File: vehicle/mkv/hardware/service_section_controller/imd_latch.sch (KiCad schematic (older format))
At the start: 36 parts, among them J301 UF_5_VT, K301 G5Q-1A4-DC12, Q301 SSM3K333R, Q302 SSM3K333R, U301 TLV3701QDBVRG4Q1, U302 TLV3701QDBVRG4Q1, U303 CD4044BDR

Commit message: incorporated feedback from dr
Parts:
- renumbered R313 to R312, R314 to R313, R315 to R314, R312 to R315, U303 to U?
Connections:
- net labels added: +12V_IMD, +12V_SHUTDOWN
- net labels removed: 12V_IMD, 12V_SHUTDOWN
- wire segments 107 -> 106
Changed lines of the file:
@@
 Wire Wire Line
 	9800 3850 9800 3750
-Wire Wire Line
-	9500 3000 9500 3150
 Text Notes 8900 2800 0    98   ~ 0
 IMD Shutdown Relay
@@
 $EndComp
 Wire Wire Line
-	9500 4900 9500 5000
+	9500 4950 9500 5000
 $Comp
 L power:GND #PWR?
@@
 I _lim: 20mA\n
 $Comp
-L formula:R_1K R312
+L formula:R_1K R315
 U 1 1 610EBBF8
 P 9500 5150
-F 0 "R312" H 9570 5196 50  0000 L CNN
+F 0 "R315" H 9570 5196 50  0000 L CNN
 F 1 "R_1K" H 9570 5105 50  0000 L CNN
 F 2 "footprints:R_0805_OEM" H 9430 5150 50  0001 C CNN
@@
 Wire Wire Line
 	10300 3850 9800 3850
-Text GLabel 9500 4900 2    50   Input ~ 0
-12V_IMD
-Text GLabel 9500 3000 0    50   Input ~ 0
-12V_SHUTDOWN
 Text Label 8100 5000 2    50   ~ 0
 LATCH_OUTPUT
@@
 	8250 5350 8250 5400
 NoConn ~ 5650 2000
-Text Notes 5100 3100 0    50   ~ 0
+Text Notes 5050 3350 0    50   ~ 0
 Latch outputs 12V when the IMD Output is “Healthy”
 Text Notes 5900 1600 0    50   ~ 0
@@
 Wire Wire Line
 	6750 1500 6750 1400
-Wire Wire Line
-	6750 1900 6900 1900
 Connection ~ 6750 1900
 Wire Wire Line
@@
 	1    0    0    -1
 $EndComp
-Text GLabel 6900 1900 2    50   Input ~ 0
-12V_IMD
 Wire Wire Line
 	7650 2000 7650 2150
@@
 NoConn ~ 6600 2500
 $Comp
-L formula:CD4044BDR U303
+L formula:CD4044BDR U?
 U 1 1 60D455EC
 P 6350 2600
-F 0 "U303" H 6125 3525 50  0000 C CNN
+F 0 "U?" H 6125 3525 50  0000 C CNN
 F 1 "CD4044BDR" H 6125 3434 50  0000 C CNN
 F 2 "footprints:SOIC127P600X175-16N" H 5850 1850 50  0001 L BNN
@@
 NoConn ~ 5650 1900
 Wire Wire Line
-	5650 2300 4950 2300
-Text GLabel 4950 2900 2    50   Input ~ 0
-12V_IMD
+	5650 2300 5350 2300
 Wire Wire Line
 	5650 2600 5550 2600
@@
 Wire Wire Line
 	1750 3700 2350 3700
-Wire Wire Line
-	1750 3700 1475 3700
 Wire Wire Line
 	2950 3900 3275 3900
@@
 	2950 4700 2650 4700
 Wire Wire Line
-	1900 4700 2000 4700
-Wire Wire Line
 	2300 4700 2350 4700
 $Comp
@@
 	0    1    1    0
 $EndComp
-Text GLabel 1900 4700 0    50   Input ~ 0
-12V_IMD
 Wire Wire Line
 	3475 3450 3550 3450
@@
 Wire Wire Line
 	3450 3450 3475 3450
-Wire Wire Line
-	3450 3200 3450 3450
 $Comp
 L formula:C_0.1uF C303
@@
 	0    1    1    0
 $EndComp
-Text GLabel 3450 3200 0    50   Input ~ 0
-12V_IMD
-Wire Wire Line
-	1475 3900 1700 3900
-Text GLabel 1700 3900 2    50   Input ~ 0
-12V_IMD
-Wire Wire Line
-	1475 4000 2000 4000
-Wire Wire Line
-	2000 4150 2000 4000
-$Comp
-L formula:UF_5_VT J301
-U 1 1 610EBAFC
-P 1125 3900
-F 0 "J301" H 1233 4337 60  0000 C CNN
-F 1 "UF_5_VT" H 1233 4231 60  0000 C CNN
-F 2 "footprints:Ultrafit_5" H 1025 4150 60  0001 C CNN
-F 3 "http://www.literature.molex.com/SQLImages/kelmscott/Molex/PDF_Images/987651-1008.pdf" H 1125 4250 60  0001 C CNN
-F 4 "DK" H 1125 3900 60  0001 C CNN "MFN"
-F 5 "WM11667-ND" H 1125 3900 60  0001 C CNN "MPN"
-F 6 "https://www.digikey.com/product-detail/en/molex-llc/1722861105/WM11667-ND/5360132" H 1625 4750 60  0001 C CNN "PurchasingLink"
-	1    1125 3900
-	1    0    0    -1
-$EndComp
 Text Notes 1350 4100 1    50   ~ 0
 This is IMD\n\n
@@
 	2350 3850 2350 3700
 Wire Wire Line
-	1825 4150 1825 4100
-$Comp
-L power:GND #PWR?
-U 1 1 610EBB0C
-P 2000 4150
-F 0 "#PWR?" H 2000 3900 50  0001 C CNN
-F 1 "GND" H 2005 3977 50  0000 C CNN
-F 2 "" H 2000 4150 50  0001 C CNN
-F 3 "" H 2000 4150 50  0001 C CNN
-	1    2000 4150
-	1    0    0    -1
-$EndComp
-$Comp
-L power:GND #PWR?
-U 1 1 610EBB06
-P 1825 4150
-F 0 "#PWR?" H 1825 3900 50  0001 C CNN
-F 1 "GND" H 1830 3977 50  0000 C CNN
-F 2 "" H 1825 4150 50  0001 C CNN
-F 3 "" H 1825 4150 50  0001 C CNN
-	1    1825 4150
-	1    0    0    -1
-$EndComp
-Wire Wire Line
 	2175 3800 2175 4150
-Wire Wire Line
-	1475 4100 1825 4100
-Wire Wire Line
-	1475 3800 2175 3800
 $Comp
 L power:GND #PWR?
@@
 	2100 1150 2150 1150
 Wire Wire Line
-	3400 1450 3400 1750
-Text GLabel 3400 1450 0    50   Input ~ 0
-12V_IMD
-Wire Wire Line
-	1400 2050 1525 2050
-Wire Wire Line
-	1500 1150 1400 1150
-Text GLabel 1400 1150 0    50   Input ~ 0
-12V_IMD
-Text GLabel 1400 2050 0    50   Input ~ 0
-12V_IMD
+	1250 2050 1525 2050
+Wire Wire Line
+	1500 1150 1250 1150
 Wire Wire Line
 	2125 2050 2250 2050
@@
 	9050 3850 9050 3650
 $Comp
-L formula:R_1.13K R315
+L formula:R_1.13K R314
 U 1 1 60D069DE
 P 8750 6050
-F 0 "R315" H 8820 6096 50  0000 L CNN
+F 0 "R314" H 8820 6096 50  0000 L CNN
 F 1 "R_1.13K" H 8820 6005 50  0000 L CNN
 F 2 "footprints:R_0805_OEM" H 8680 6050 50  0001 C CNN
@@
 	8250 5000 8750 5000
 $Comp
-L formula:R_2.2K R313
+L formula:R_2.2K R312
 U 1 1 60D03BAD
 P 8750 5200
-F 0 "R313" H 8820 5246 50  0000 L CNN
+F 0 "R312" H 8820 5246 50  0000 L CNN
 F 1 "R_2.2K" H 8820 5155 50  0000 L CNN
 F 2 "footprints:R_0805_OEM" H 8680 5200 50  0001 C CNN
@@
 $EndComp
 $Comp
-L formula:R_1K R314
+L formula:R_1K R313
 U 1 1 60DAD819
 P 8750 5550
-F 0 "R314" H 8820 5596 50  0000 L CNN
+F 0 "R313" H 8820 5596 50  0000 L CNN
 F 1 "R_1K" H 8820 5505 50  0000 L CNN
 F 2 "footprints:R_0805_OEM" H 8680 5550 50  0001 C CNN
@@
 Wire Wire Line
 	4750 2200 5650 2200
-Wire Wire Line
-	4950 2300 4950 2900
 Wire Wire Line
 	4750 2200 4750 3800
@@
 U 1 1 6147DE08
 P 2650 2000
-F 0 "TP302" V 2650 2250 50  0000 C CNN
+F 0 "TP302" V 2650 2300 50  0000 C CNN
 F 1 "Test_Point_SMD" V 2550 2050 50  0000 C CNN
 F 2 "TestPoint:TestPoint_Pad_D1.0mm" H 2650 1850 50  0001 C CNN
@@
 Wire Wire Line
 	9800 2950 9800 3150
+Wire Wire Line
+	1475 3800 2175 3800
+Wire Wire Line
+	1750 3700 1475 3700
+$Comp
+L formula:UF_5_VT J301
+U 1 1 610EBAFC
+P 1125 3900
+F 0 "J301" H 1233 4337 60  0000 C CNN
+F 1 "UF_5_VT" H 1233 4231 60  0000 C CNN
+F 2 "footprints:Ultrafit_5" H 1025 4150 60  0001 C CNN
+F 3 "http://www.literature.molex.com/SQLImages/kelmscott/Molex/PDF_Images/987651-1008.pdf" H 1125 4250 60  0001 C CNN
+F 4 "DK" H 1125 3900 60  0001 C CNN "MFN"
+F 5 "WM11667-ND" H 1125 3900 60  0001 C CNN "MPN"
+F 6 "https://www.digikey.com/product-detail/en/molex-llc/1722861105/WM11667-ND/5360132" H 1625 4750 60  0001 C CNN "PurchasingLink"
+	1    1125 3900
+	1    0    0    -1
+$EndComp
+$Comp
+L power:GND #PWR?
+U 1 1 61A9CFCE
+P 1600 4150
+F 0 "#PWR?" H 1600 3900 50  0001 C CNN
+F 1 "GND" H 1605 3977 50  0000 C CNN
+F 2 "" H 1600 4150 50  0001 C CNN
+F 3 "" H 1600 4150 50  0001 C CNN
+	1    1600 4150
+	1    0    0    -1
+$EndComp
+Wire Wire Line
+	1600 4100 1600 4150
+Wire Wire Line
+	1475 4100 1600 4100
+Wire Wire Line
+	1750 4150 1750 4000
+Wire Wire Line
+	1750 4000 1475 4000
+Wire Wire Line
+	1475 3900 1700 3900
+Wire Wire Line
+	1800 4700 2000 4700
+Wire Wire Line
+	6750 1900 7650 1900
+$Comp
+L formula:+12V_IMD #PWR?
+U 1 1 61AF5615
+P 9500 4950
+F 0 "#PWR?" H 9500 4800 50  0001 C CNN
+F 1 "+12V_IMD" H 9515 5123 50  0000 C CNN
+F 2 "" H 9500 4950 50  0001 C CNN
+F 3 "" H 9500 4950 50  0001 C CNN
+	1    9500 4950
+	1    0    0    -1
+$EndComp
+Text GLabel 1250 1150 0    50   Input ~ 0
++12V_IMD
+Text GLabel 3400 1400 2    50   Input ~ 0
++12V_IMD
+Wire Wire Line
+	3400 1400 3400 1750
+Text GLabel 1250 2050 0    50   Input ~ 0
++12V_IMD
+Text GLabel 1700 3900 2    50   Input ~ 0
++12V_IMD
+$Comp
+L power:GND #PWR?
+U 1 1 610EBB0C
+P 1750 4150
+F 0 "#PWR?" H 1750 3900 50  0001 C CNN
+F 1 "GND" H 1755 3977 50  0000 C CNN
+F 2 "" H 1750 4150 50  0001 C CNN
+F 3 "" H 1750 4150 50  0001 C CNN
+	1    1750 4150
+	1    0    0    -1
+$EndComp
+Text GLabel 3450 3050 2    50   Input ~ 0
++12V_IMD
+Wire Wire Line
+	3450 3050 3450 3450
+Text GLabel 1800 4700 0    50   Input ~ 0
++12V_IMD
+Text GLabel 5350 2300 0    50   Input ~ 0
++12V_IMD
+Text GLabel 7650 1900 2    50   Input ~ 0
++12V_IMD
+Text GLabel 9500 3000 0    50   Input ~ 0
++12V_SHUTDOWN
+Wire Wire Line
+	9500 3000 9500 3150
 $EndSCHEMATC

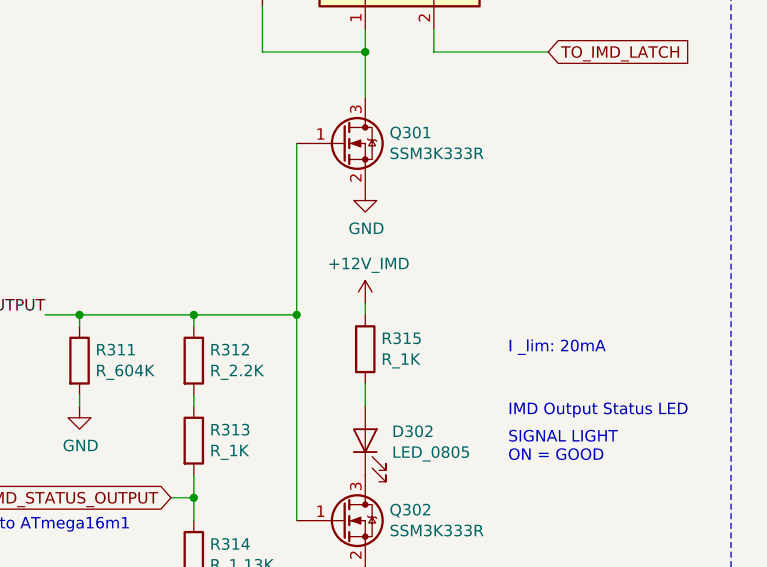
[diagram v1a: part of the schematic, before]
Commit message: complete service section controller layout, need to change some test point labels though
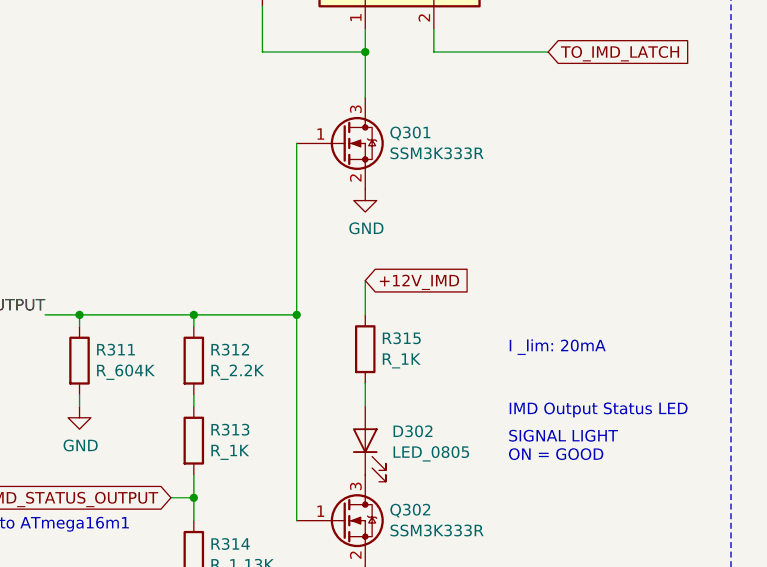
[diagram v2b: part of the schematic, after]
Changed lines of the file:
@@
 $EndComp
 Wire Wire Line
-	9500 4950 9500 5000
+	9500 4850 9500 5000
 $Comp
 L power:GND #PWR?
@@
 Wire Wire Line
 	6750 1900 7650 1900
-$Comp
-L formula:+12V_IMD #PWR?
-U 1 1 61AF5615
-P 9500 4950
-F 0 "#PWR?" H 9500 4800 50  0001 C CNN
-F 1 "+12V_IMD" H 9515 5123 50  0000 C CNN
-F 2 "" H 9500 4950 50  0001 C CNN
-F 3 "" H 9500 4950 50  0001 C CNN
-	1    9500 4950
-	1    0    0    -1
-$EndComp
 Text GLabel 1250 1150 0    50   Input ~ 0
 +12V_IMD
@@
 Wire Wire Line
 	9500 3000 9500 3150
+Text GLabel 9500 4850 2    50   Input ~ 0
++12V_IMD
 $EndSCHEMATC

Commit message: Made changes for Rev 2 of SS controller schematic and layout
changed 12V IMD net to 5V IMD
to make layout changes easier, 5V IMD is supplied after 5V AIR control fuse
Power Main: Added larger test points for +Batt and GND for easier testing
IMD Latch: changed 12V nets to 5V, swapped inverting and non-inverting inputs for both op amps, removed resistor divider at IMD_STATUS_OUTPUT that goes to the ATmega
TSAL/AIL: changed 12V_TSAL to a 5V input, changed ts+ side resistor dividers to 1k and 120 (bottom of the op amp), changed AIL logic to use an nmos
Power Secondary: removed HV lin reg, added 15V - 5V lin reg and added a fuse for the 5V output. 400-15V lin reg can be used to provide 15V OR we can change resistors to provide 5V and short the output of lin reg to the output of the buck.
Micros: added a programming header for isospi for easier firmware testing, added test points for CANH and CANL for firmware debugging.
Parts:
- removed R312: R_2.2K, footprints:R_0805_OEM, symbol formula:R_2.2K
- removed R313: R_1K, footprints:R_0805_OEM, symbol formula:R_1K
- removed R314: R_1.13K, footprints:R_0805_OEM, symbol formula:R_1.13K
- added R312: R_3K, footprints:R_0805_OEM, symbol formula:R_3K
- TP307: value Test_Point_SMD -> LATCH_OUTPUT
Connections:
- net labels added: +5V_IMD
- net labels removed: +12V_IMD
- wire segments 106 -> 108
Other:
- note added: "DELAY SIDE:\ntimer gives the IMD time \nto power up"
- note added: "Latch outputs 5V when the IMD Output is “Healthy”"
- note added: "Vout = 1.67V"
- note added: "“GOOD” Output is Logical High in a range of 0V-12V; Threshold set to +1.67V\n"
- note removed: "DELAY SIDE:\ntimer gives the IMD time to power up"
- note removed: "Latch outputs 12V when the IMD Output is “Healthy”"
- note removed: "Vout = 8V"
- note removed: "“GOOD” Output is Logical High in a range of 0V-12V; Threshold set to +8V\n"
- moved on the sheet: C301, J301, R301, R302, R303, R304, R305, R306, R307, R308, R309, R310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
